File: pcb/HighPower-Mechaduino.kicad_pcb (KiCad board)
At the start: 2 copper layers, 60 x 60 mm, 133 parts, among them J1 SUPPLY, J2 STEPPER, P1 SWD, P2 USB, P3 PoStep25-32, P4 CONN_01X04, Q1 SSM3J328R, Q10 IPD079N06L3G, Q11 BSS138, Q2 BSS138, Q3 IPD079N06L3G, Q4 IPD079N06L3G, Q5 IPD079N06L3G, Q6 IPD079N06L3G, Q7 IPD079N06L3G, Q8 IPD079N06L3G, Q9 IPD079N06L3G, SW1 B3U-1000P, U1 AS5047D, U2 AP2112K-3.3TRG1, U3 AT24CS64-SSHM, U4 SAMD21G18A-A, U5 A4955GLPTR-T, U6 A4955GLPTR-T, U7 USBLC6-2SC6, U8 MCP16331T, U9 LM75BD, Y1 G83270022

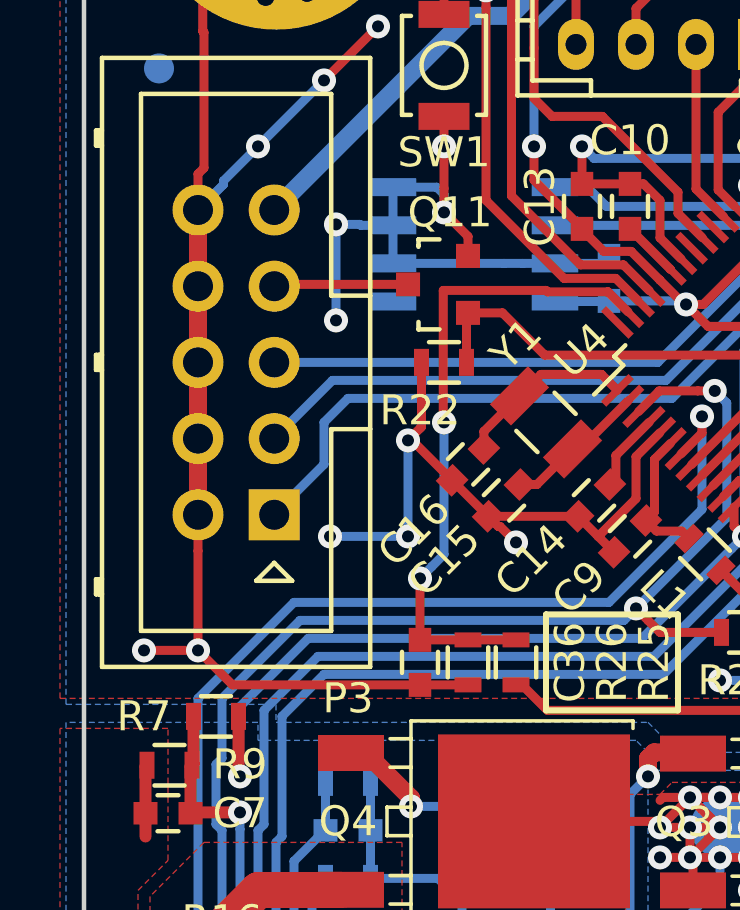
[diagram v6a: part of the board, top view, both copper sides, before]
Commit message: Fix connector footprint
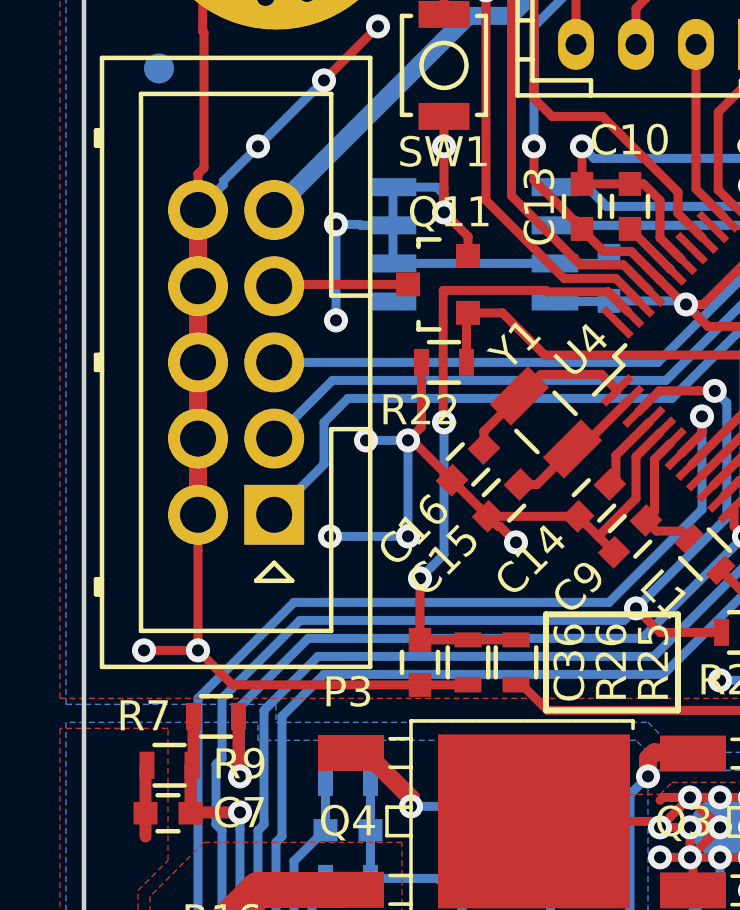
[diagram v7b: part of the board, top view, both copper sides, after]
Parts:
- P3: footprint Connectors_Multicomp:Multicomp_MC9A12-1034_2x05x2.54mm_Straight -> Connectors_On-Shore-Technology:On-Shore-Technology_ED1543_2x05x2.54mm_Straight
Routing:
- net GND: track 541.5 -> 543.1 mm, vias 71 -> 72
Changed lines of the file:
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@@
     (thickness 1.6)
     (drawings 25)
-    (tracks 1560)
+    (tracks 1563)
     (zones 0)
     (modules 133)
@@
     (46 B.CrtYd user)
     (47 F.CrtYd user)
-    (48 B.Fab user hide)
-    (49 F.Fab user hide)
+    (48 B.Fab user)
+    (49 F.Fab user)
   )
   (setup
@@
     (add_net /PWM_Bridge_A4955-B/OUT2)
   )
+  (module Connectors_On-Shore-Technology:On-Shore-Technology_ED1543_2x05x2.54mm_Straight (layer F.Cu)
+    (at 126.34 96.88 90)
+    (descr http://www.farnell.com/datasheets/1520732.pdf)
+    (tags "connector multicomp MC9A MC9A12")
+    (fp_text reference P3 (at -5.92 2.46 180) (layer F.SilkS)
+      (effects (font (size 1 1) (thickness 0.15)))
+    )
+    (fp_text value PoStep25-32 (at 5.08 5 90) (layer F.Fab)
+      (effects (font (size 1 1) (thickness 0.15)))
+    )
+    (fp_line (start -5.07 3.2) (end -5.07 -5.74) (layer F.SilkS) (width 0.15))
+    (fp_line (start -5.07 -5.74) (end 15.23 -5.74) (layer F.SilkS) (width 0.15))
+    (fp_line (start 15.23 -5.74) (end 15.23 3.2) (layer F.SilkS) (width 0.15))
+    (fp_line (start 15.23 3.2) (end -5.07 3.2) (layer F.SilkS) (width 0.15))
+    (fp_line (start 2.855 3.2) (end 2.855 1.9) (layer F.SilkS) (width 0.15))
+    (fp_line (start 2.855 1.9) (end -3.87 1.9) (layer F.SilkS) (width 0.15))
+    (fp_line (start -3.87 1.9) (end -3.87 -4.44) (layer F.SilkS) (width 0.15))
+    (fp_line (start -3.87 -4.44) (end 14.03 -4.44) (layer F.SilkS) (width 0.15))
+    (fp_line (start 14.03 -4.44) (end 14.03 1.9) (layer F.SilkS) (width 0.15))
+    (fp_line (start 14.03 1.9) (end 7.305 1.9) (layer F.SilkS) (width 0.15))
+    (fp_line (start 7.305 1.9) (end 7.305 3.2) (layer F.SilkS) (width 0.15))
+    (fp_line (start 4.83 -5.74) (end 4.83 -5.94) (layer F.SilkS) (width 0.15))
+    (fp_line (start 4.83 -5.94) (end 5.33 -5.94) (layer F.SilkS) (width 0.15))
+    (fp_line (start 5.33 -5.94) (end 5.33 -5.74) (layer F.SilkS) (width 0.15))
+    (fp_line (start 4.83 -5.84) (end 5.33 -5.84) (layer F.SilkS) (width 0.15))
+    (fp_line (start 12.31 -5.74) (end 12.31 -5.94) (layer F.SilkS) (width 0.15))
+    (fp_line (start 12.31 -5.94) (end 12.81 -5.94) (layer F.SilkS) (width 0.15))
+    (fp_line (start 12.81 -5.94) (end 12.81 -5.74) (layer F.SilkS) (width 0.15))
+    (fp_line (start 12.31 -5.84) (end 12.81 -5.84) (layer F.SilkS) (width 0.15))
+    (fp_line (start -2.65 -5.74) (end -2.65 -5.94) (layer F.SilkS) (width 0.15))
+    (fp_line (start -2.65 -5.94) (end -2.15 -5.94) (layer F.SilkS) (width 0.15))
+    (fp_line (start -2.15 -5.94) (end -2.15 -5.74) (layer F.SilkS) (width 0.15))
+    (fp_line (start -2.65 -5.84) (end -2.15 -5.84) (layer F.SilkS) (width 0.15))
+    (fp_line (start -2.2 0.6) (end -2.2 -0.6) (layer F.SilkS) (width 0.15))
+    (fp_line (start -2.2 -0.6) (end -1.6 0) (layer F.SilkS) (width 0.15))
+    (fp_line (start -1.6 0) (end -2.2 0.6) (layer F.SilkS) (width 0.15))
+    (fp_line (start -5.55 3.7) (end -5.55 -6.25) (layer F.CrtYd) (width 0.05))
+    (fp_line (start -5.55 -6.25) (end 15.75 -6.25) (layer F.CrtYd) (width 0.05))
+    (fp_line (start 15.75 -6.25) (end 15.75 3.7) (layer F.CrtYd) (width 0.05))
+    (fp_line (start 15.75 3.7) (end -5.55 3.7) (layer F.CrtYd) (width 0.05))
+    (pad 1 thru_hole rect (at 0 0 90) (size 2 2) (drill 1.2) (layers *.Cu *.Mask)
+      (net 24 /STP_EN))
+    (pad 2 thru_hole circle (at 0 -2.54 90) (size 2 2) (drill 1.2) (layers *.Cu *.Mask)
+      (net 1 GND))
+    (pad 3 thru_hole circle (at 2.54 0 90) (size 2 2) (drill 1.2) (layers *.Cu *.Mask)
+      (net 25 /STP_DIR))
+    (pad 4 thru_hole circle (at 2.54 -2.54 90) (size 2 2) (drill 1.2) (layers *.Cu *.Mask)
+      (net 1 GND))
+    (pad 5 thru_hole circle (at 5.08 0 90) (size 2 2) (drill 1.2) (layers *.Cu *.Mask)
+      (net 26 /STP_STEP))
+    (pad 6 thru_hole circle (at 5.08 -2.54 90) (size 2 2) (drill 1.2) (layers *.Cu *.Mask)
+      (net 1 GND))
+    (pad 7 thru_hole circle (at 7.62 0 90) (size 2 2) (drill 1.2) (layers *.Cu *.Mask)
+      (net 77 "Net-(P3-Pad7)"))
+    (pad 8 thru_hole circle (at 7.62 -2.54 90) (size 2 2) (drill 1.2) (layers *.Cu *.Mask)
+      (net 1 GND))
+    (pad 9 thru_hole circle (at 10.16 0 90) (size 2 2) (drill 1.2) (layers *.Cu *.Mask)
+      (net 4 +5V))
+    (pad 10 thru_hole circle (at 10.16 -2.54 90) (size 2 2) (drill 1.2) (layers *.Cu *.Mask)
+      (net 1 GND))
+  )
   (module Resistors_SMD:R_0603 (layer F.Cu)
     (at 135 77 270)
@@
       (net 27 "Net-(L2-Pad1)"))
   )
-  (module Connectors_Multicomp:Multicomp_MC9A12-1034_2x05x2.54mm_Straight (layer F.Cu)
-    (at 126.34 96.88 90)
-    (descr http://www.farnell.com/datasheets/1520732.pdf)
-    (tags "connector multicomp MC9A MC9A12")
-    (fp_text reference P3 (at -6.12 2.46 180) (layer F.SilkS)
-      (effects (font (size 1 1) (thickness 0.15)))
-    )
-    (fp_text value PoStep25-32 (at 5.08 -7.94 90) (layer F.Fab)
-      (effects (font (size 1 1) (thickness 0.15)))
-    )
-    (fp_line (start 15.75 3.7) (end -5.55 3.7) (layer F.CrtYd) (width 0.05))
-    (fp_line (start 15.75 -6.25) (end 15.75 3.7) (layer F.CrtYd) (width 0.05))
-    (fp_line (start -5.55 -6.25) (end 15.75 -6.25) (layer F.CrtYd) (width 0.05))
-    (fp_line (start -5.55 3.7) (end -5.55 -6.25) (layer F.CrtYd) (width 0.05))
-    (fp_line (start -1.6 0) (end -2.2 0.6) (layer F.SilkS) (width 0.15))
-    (fp_line (start -2.2 -0.6) (end -1.6 0) (layer F.SilkS) (width 0.15))
-    (fp_line (start -2.2 0.6) (end -2.2 -0.6) (layer F.SilkS) (width 0.15))
-    (fp_line (start -2.65 -5.84) (end -2.15 -5.84) (layer F.SilkS) (width 0.15))
-    (fp_line (start -2.15 -5.94) (end -2.15 -5.74) (layer F.SilkS) (width 0.15))
-    (fp_line (start -2.65 -5.94) (end -2.15 -5.94) (layer F.SilkS) (width 0.15))
-    (fp_line (start -2.65 -5.74) (end -2.65 -5.94) (layer F.SilkS) (width 0.15))
-    (fp_line (start 12.31 -5.84) (end 12.81 -5.84) (layer F.SilkS) (width 0.15))
-    (fp_line (start 12.81 -5.94) (end 12.81 -5.74) (layer F.SilkS) (width 0.15))
-    (fp_line (start 12.31 -5.94) (end 12.81 -5.94) (layer F.SilkS) (width 0.15))
-    (fp_line (start 12.31 -5.74) (end 12.31 -5.94) (layer F.SilkS) (width 0.15))
-    (fp_line (start 4.83 -5.84) (end 5.33 -5.84) (layer F.SilkS) (width 0.15))
-    (fp_line (start 5.33 -5.94) (end 5.33 -5.74) (layer F.SilkS) (width 0.15))
-    (fp_line (start 4.83 -5.94) (end 5.33 -5.94) (layer F.SilkS) (width 0.15))
-    (fp_line (start 4.83 -5.74) (end 4.83 -5.94) (layer F.SilkS) (width 0.15))
-    (fp_line (start 7.305 1.9) (end 7.305 3.2) (layer F.SilkS) (width 0.15))
-    (fp_line (start 14.03 1.9) (end 7.305 1.9) (layer F.SilkS) (width 0.15))
-    (fp_line (start 14.03 -4.44) (end 14.03 1.9) (layer F.SilkS) (width 0.15))
-    (fp_line (start -3.87 -4.44) (end 14.03 -4.44) (layer F.SilkS) (width 0.15))
-    (fp_line (start -3.87 1.9) (end -3.87 -4.44) (layer F.SilkS) (width 0.15))
-    (fp_line (start 2.855 1.9) (end -3.87 1.9) (layer F.SilkS) (width 0.15))
-    (fp_line (start 2.855 3.2) (end 2.855 1.9) (layer F.SilkS) (width 0.15))
-    (fp_line (start 15.23 3.2) (end -5.07 3.2) (layer F.SilkS) (width 0.15))
-    (fp_line (start 15.23 -5.74) (end 15.23 3.2) (layer F.SilkS) (width 0.15))
-    (fp_line (start -5.07 -5.74) (end 15.23 -5.74) (layer F.SilkS) (width 0.15))
-    (fp_line (start -5.07 3.2) (end -5.07 -5.74) (layer F.SilkS) (width 0.15))
-    (pad 1 thru_hole rect (at 0 0 90) (size 1.7 1.7) (drill 1) (layers *.Cu *.Mask F.SilkS)
-      (net 24 /STP_EN))
-    (pad 2 thru_hole circle (at 0 -2.54 90) (size 1.7 1.7) (drill 1) (layers *.Cu *.Mask F.SilkS)
-      (net 1 GND))
-    (pad 3 thru_hole circle (at 2.54 0 90) (size 1.7 1.7) (drill 1) (layers *.Cu *.Mask F.SilkS)
-      (net 25 /STP_DIR))
-    (pad 4 thru_hole circle (at 2.54 -2.54 90) (size 1.7 1.7) (drill 1) (layers *.Cu *.Mask F.SilkS)
-      (net 1 GND))
-    (pad 5 thru_hole circle (at 5.08 0 90) (size 1.7 1.7) (drill 1) (layers *.Cu *.Mask F.SilkS)
-      (net 26 /STP_STEP))
-    (pad 6 thru_hole circle (at 5.08 -2.54 90) (size 1.7 1.7) (drill 1) (layers *.Cu *.Mask F.SilkS)
-      (net 1 GND))
-    (pad 7 thru_hole circle (at 7.62 0 90) (size 1.7 1.7) (drill 1) (layers *.Cu *.Mask F.SilkS)
-      (net 77 "Net-(P3-Pad7)"))
-    (pad 8 thru_hole circle (at 7.62 -2.54 90) (size 1.7 1.7) (drill 1) (layers *.Cu *.Mask F.SilkS)
-      (net 1 GND))
-    (pad 9 thru_hole circle (at 10.16 0 90) (size 1.7 1.7) (drill 1) (layers *.Cu *.Mask F.SilkS)
-      (net 4 +5V))
-    (pad 10 thru_hole circle (at 10.16 -2.54 90) (size 1.7 1.7) (drill 1) (layers *.Cu *.Mask F.SilkS)
-      (net 1 GND))
-  )
   (module TO_SOT_Packages_SMD:SOT-23 (layer F.Cu)
     (at 155.4 75.2)
@@
   (gr_line (start 123 70) (end 177 70) (layer Edge.Cuts) (width 0.15))
   (segment (start 139 72) (end 139 70.6) (width 0.3) (layer Dwgs.User) (net 0))
+  (segment (start 130.8 94.4) (end 129.4 94.4) (width 0.3) (layer B.Cu) (net 1))
+  (segment (start 129.2 94.4) (end 129.4 94.4) (width 0.3) (layer B.Cu) (net 1))
+  (via (at 129.4 94.4) (size 0.8) (drill 0.4) (layers F.Cu B.Cu) (net 1))
   (segment (start 138.4 81.2) (end 138.4 80) (width 0.3) (layer F.Cu) (net 1))
   (segment (start 139.6 78.8) (end 140.8 78.8) (width 0.3) (layer F.Cu) (net 1))

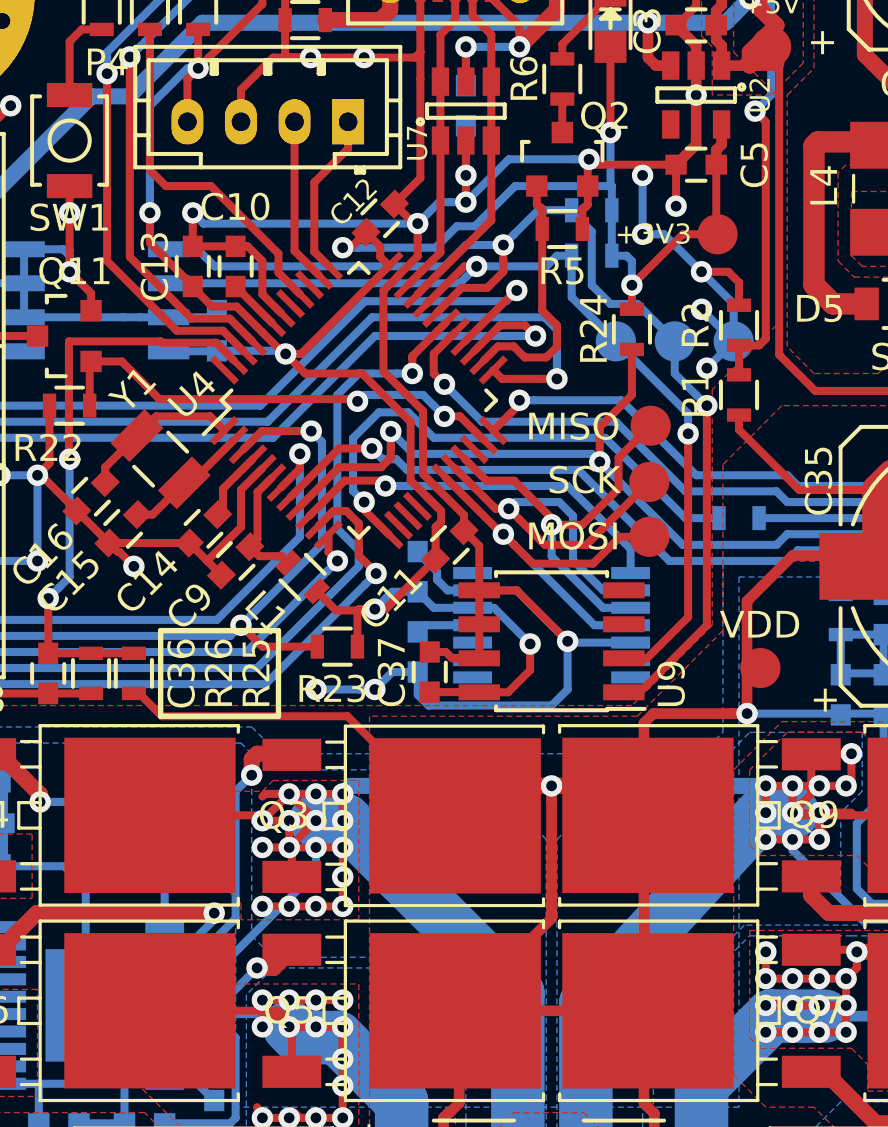
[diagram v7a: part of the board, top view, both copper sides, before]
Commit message: Remove connection to SLEEPn Pin
I think we don't have to connect this pin, and if yes we can fix it manually on the prototype

The support of Alegro wasn't very helpful about that topic
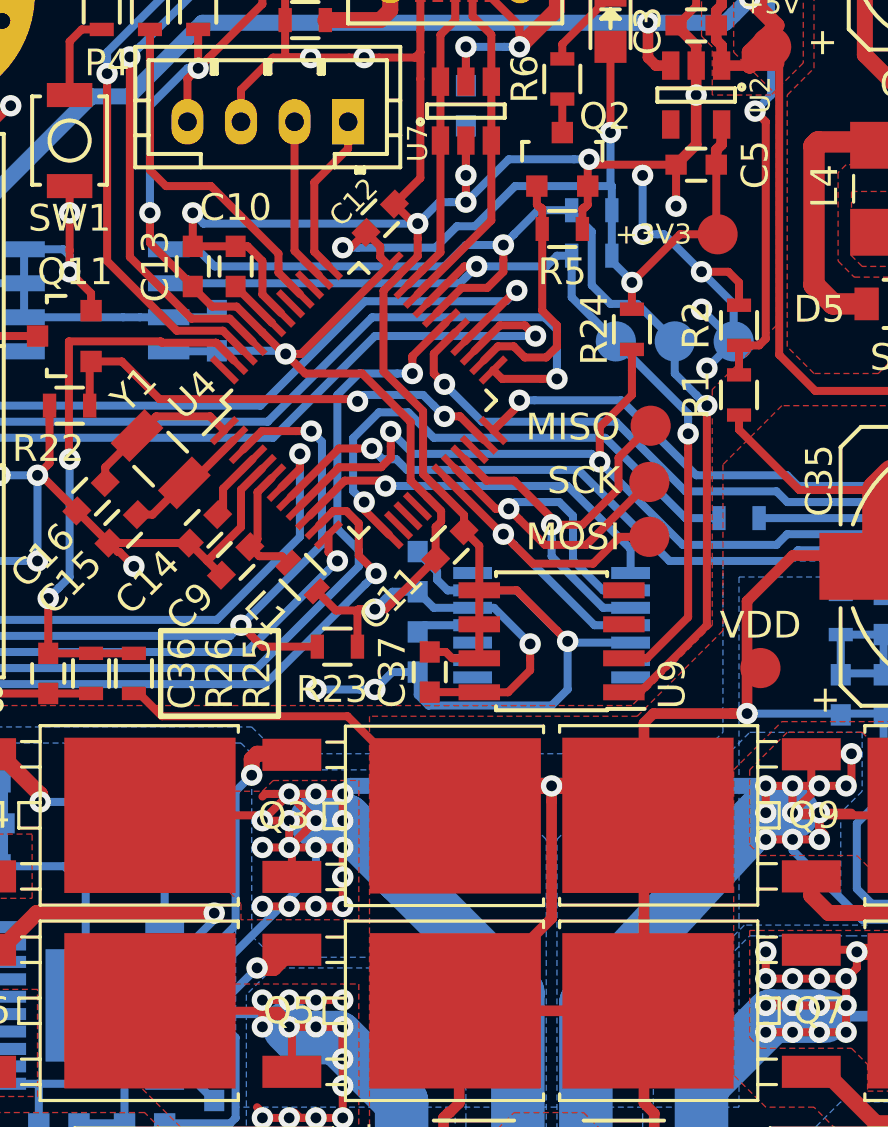
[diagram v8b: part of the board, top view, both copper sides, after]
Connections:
- U5 pad 9: /SLEEP -> /PWM_Bridge_A4955-A/SLEEPn
- U6 pad 9: /SLEEP -> /PWM_Bridge_A4955-B/SLEEPn
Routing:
- net +3V3: track 99.9 -> 99.4 mm
